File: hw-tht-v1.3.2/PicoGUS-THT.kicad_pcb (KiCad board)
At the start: 2 copper layers, 101.9 x 99.8 mm, 88 parts, among them J1 IRQDMA_JP, J11 USB-A, J3 Bus_ISA_8bit, J5 SJ1-3535NG, J6 UART_TX, J7 USB power jumper, J8 SJ1-3535NG-GR, J9 Waveblaster, U1 Pico, U10 74AHCT126, U11 NE5532, U12 USBLC6-2SC6, U2 74AHC244, U3 SN74CB3T3257, U4 SN74CB3T3257, U5 74AHC14, U6 74AHC00, U7 74AHC00, U8 APS6404L-3SQR-SN, U9 PCM5100A

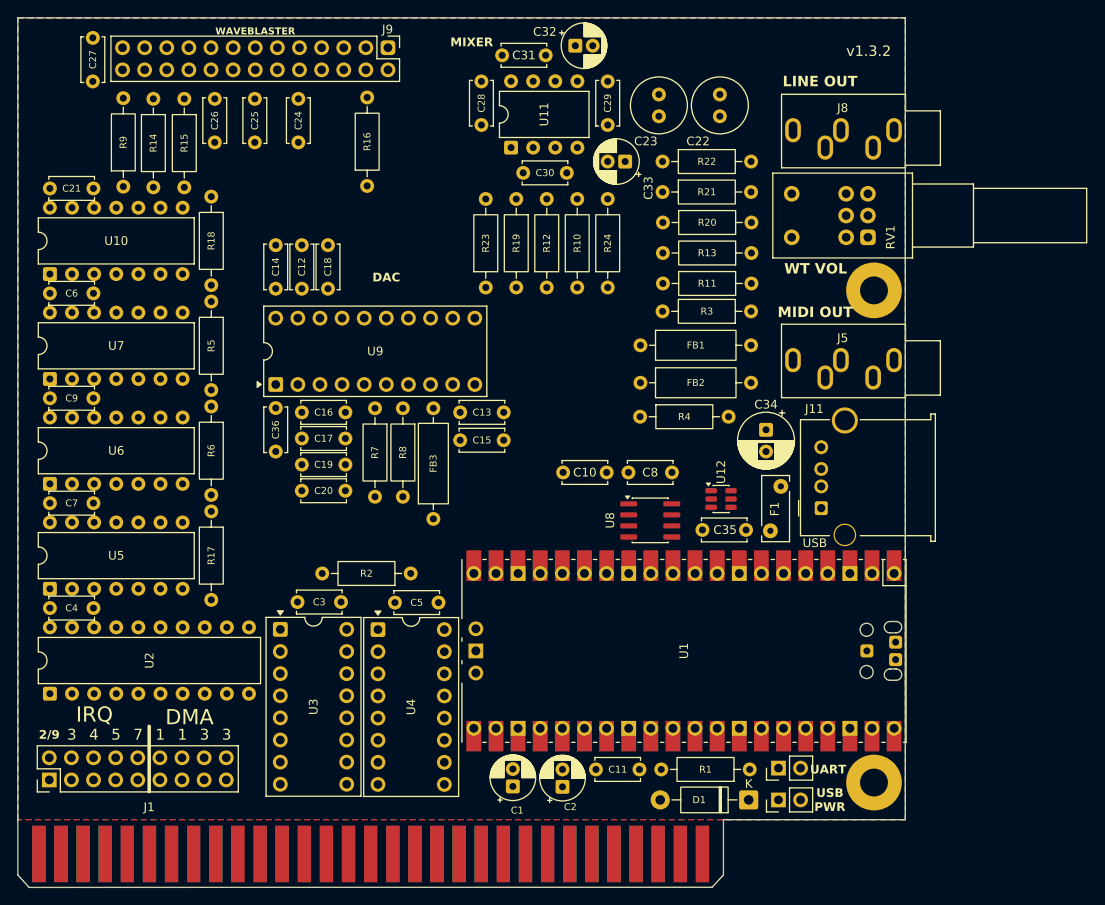
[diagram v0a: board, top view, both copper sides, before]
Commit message: THT v1.3.2: route the 102 mm board
Two-layer route of the 102 mm placement: grid router, then a polish pass
and two review rounds (analog/power and digital/ISA/USB/manufacturing),
each fixed and re-measured against the 103.7 mm layout of 8dbb6c6.

- I2S and the other digital nets kept out of the DAC analog half and
  1 mm from all audio copper; FB3 (AVDD) on its own +3V3 feed
- ±12V >= 0.30 mm from non-GND THT pads and from the bare gold fingers;
  vias >= 0.30 mm from other-net pads, none near the fingers
- mixer output re-routed so the back pour ties U11 to the line-out sleeve
- USB D+/D- flow-through U12, clear of C35 and the Pico NPTH peg hole
- power widened up to 0.8 mm, GND stitching, island vias

DRC with schematic parity: 0 unconnected, errors only the 12 accepted
courtyard overlaps (export with FORCE=1). README: routing notes, review
fixes, comparison table and accepted weak points.

Co-Authored-By: Claude Opus 5.5 <noreply@anthropic.com>
Claude-Session: https://claude.ai/code/session_011utN3x8yYUNDvkpGCEq5yD
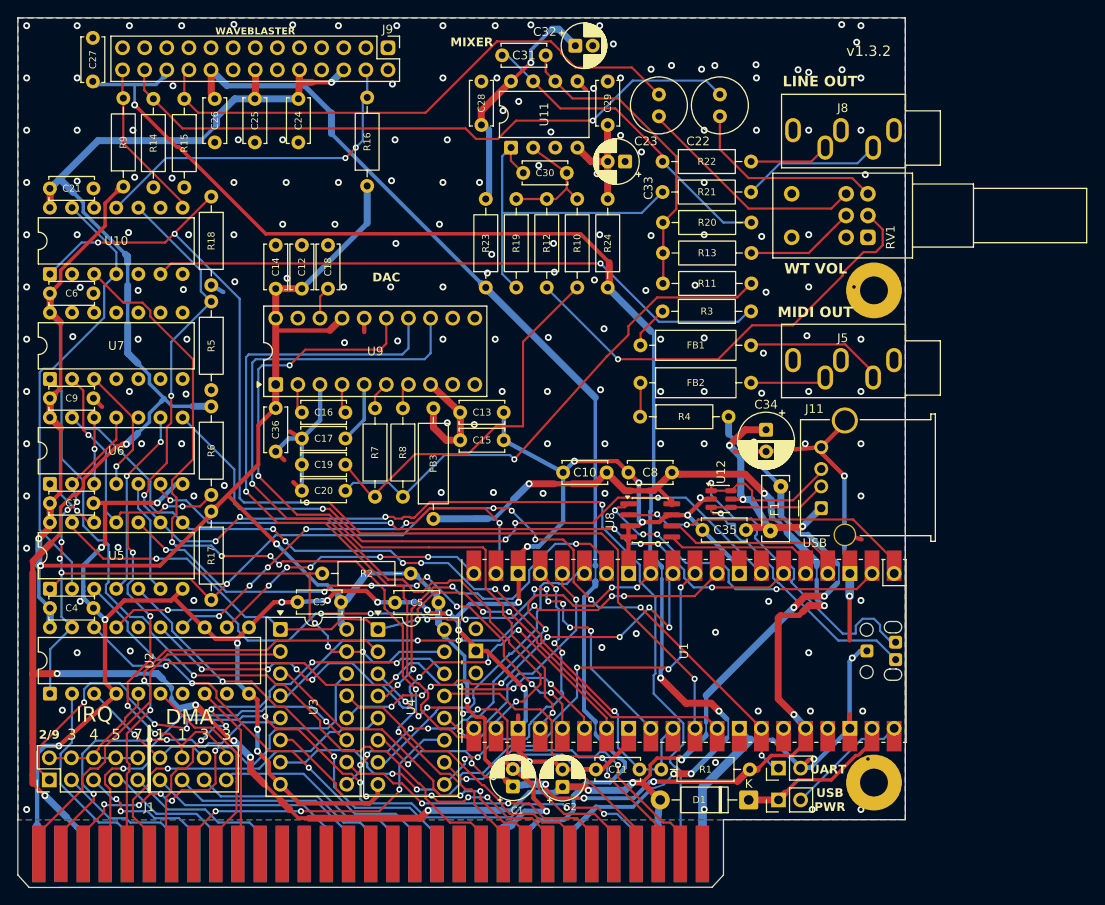
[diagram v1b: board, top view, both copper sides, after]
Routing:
- net GND: track 0.00 -> 382.6 mm, vias 0 -> 194
- net +3V3: track 0.00 -> 315.5 mm, vias 0 -> 11
- net +5V: track 0.00 -> 290.9 mm, vias 0 -> 13
- net -12V: track 0.00 -> 158.9 mm, vias 0 -> 5
- net RESET: track 0.00 -> 140.5 mm, vias 0 -> 6
- net ~{RI/OCHRDY}: track 0.00 -> 125.8 mm, vias 0 -> 4
- net +12V: track 0.00 -> 125.2 mm
- net UART_TX: track 0.00 -> 106.1 mm, vias 0 -> 7
- net I/OCHRDY: track 0.00 -> 101.5 mm, vias 0 -> 6
- net RUN: track 0.00 -> 93.9 mm, vias 0 -> 6
- net BCK: track 0.00 -> 91.9 mm, vias 0 -> 2
- net ~{BUSOE}: track 0.00 -> 90.3 mm, vias 0 -> 8
- net ADS: track 0.00 -> 89.1 mm, vias 0 -> 4
- net IRQ2: track 0.00 -> 88.3 mm, vias 0 -> 7
- net LRCK: track 0.00 -> 85.0 mm, vias 0 -> 3
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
